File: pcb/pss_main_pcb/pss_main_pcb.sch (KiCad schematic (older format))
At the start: 44 parts

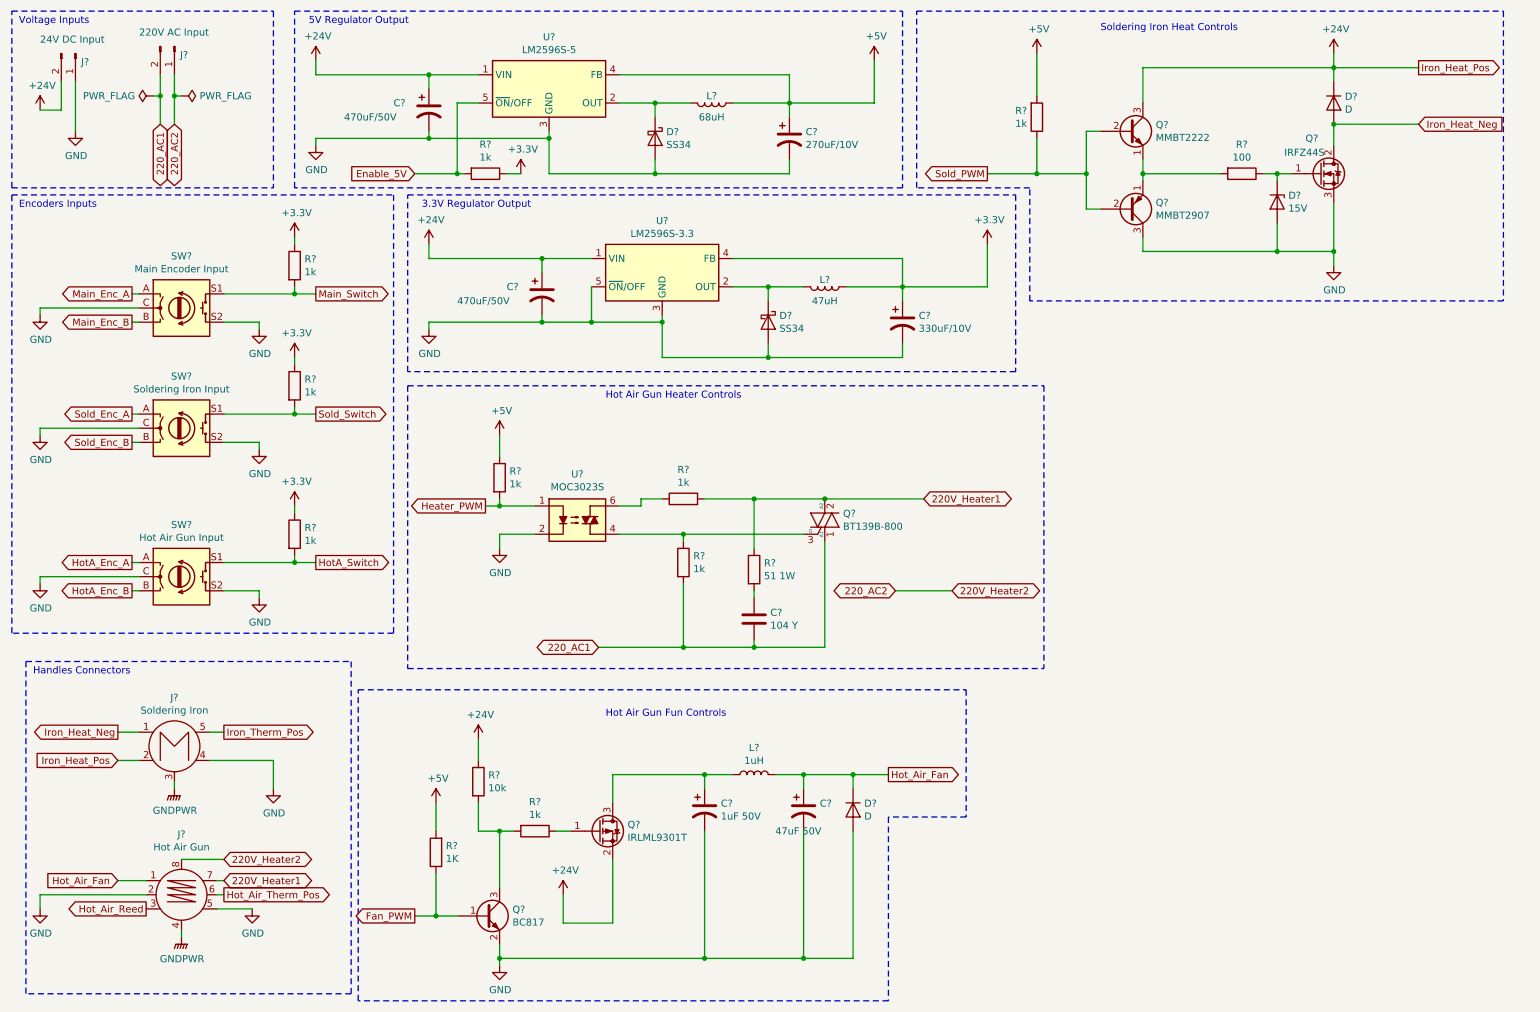
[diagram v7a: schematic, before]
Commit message: Add thermocouple feedback schematics
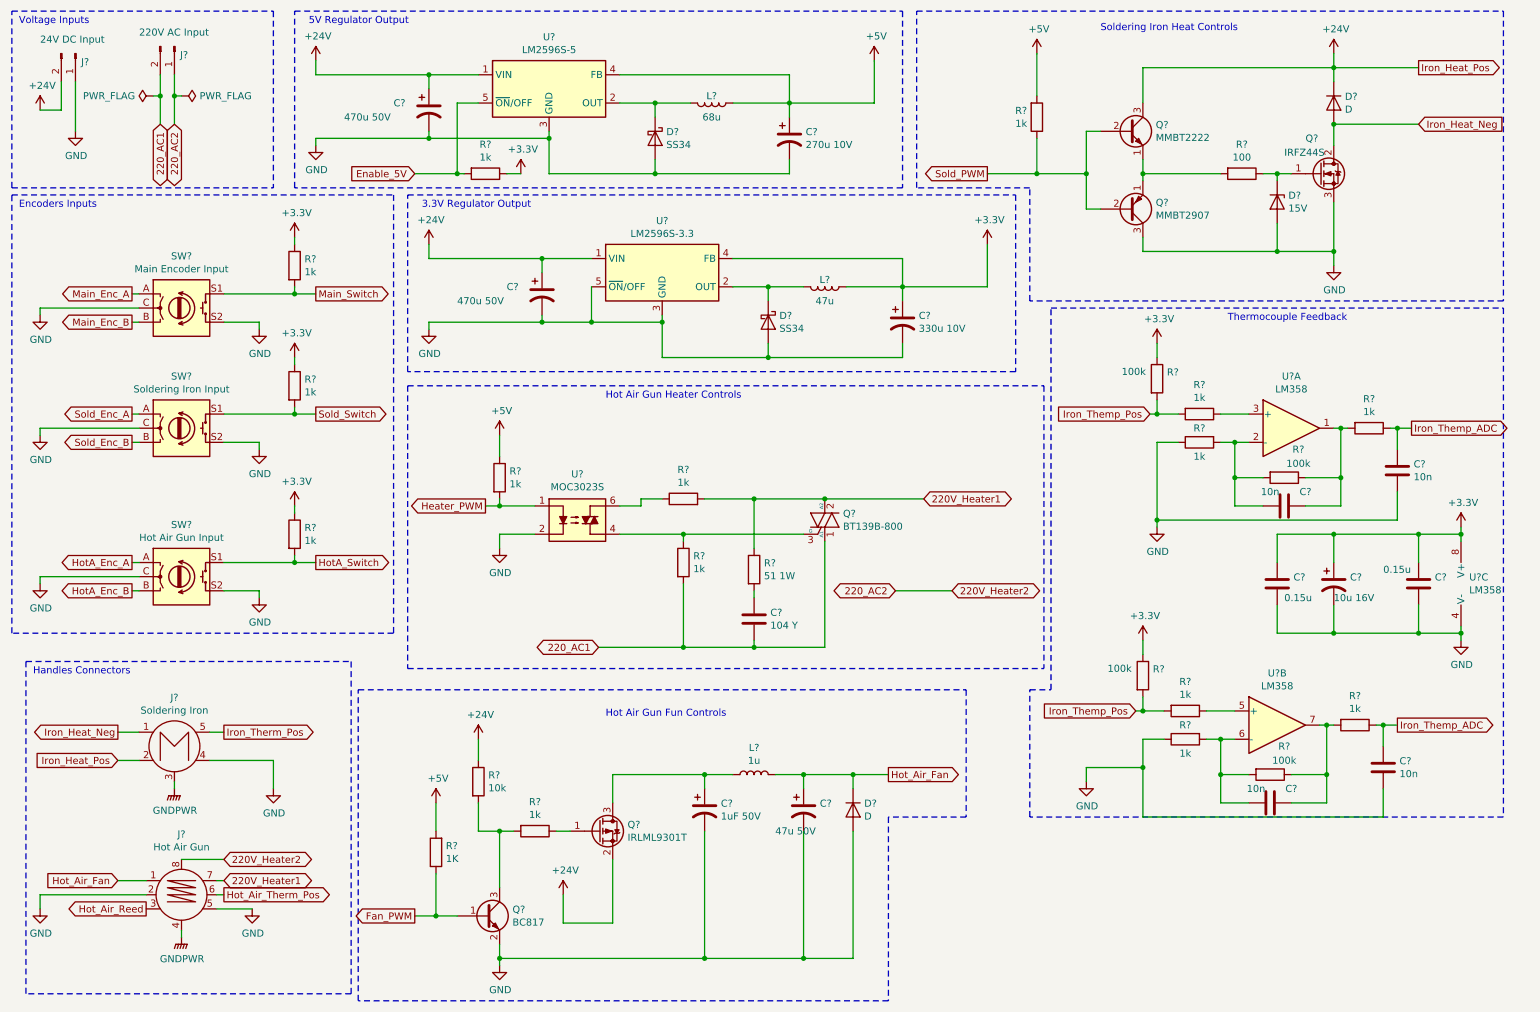
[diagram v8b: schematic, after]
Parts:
- added C? (x2): 0.15u, symbol Device:C
- added C? (x4): 10n, symbol Device:C
- added C?: 10u 16V, symbol Device:CP1
- added R? (x6): 1k, symbol Device:R
- added R? (x4): 100k, symbol Device:R
- added U? (x3): LM358, symbol Amplifier_Operational:LM358
- C? (x2): value 470uF/50V -> 470u 50V
- C?: value 270uF/10V -> 270u 10V
- C?: value 330uF/10V -> 330u 10V
- C?: value 47uF 50V -> 47u 50V
- L?: value 68uH -> 68u
- L?: value 47uH -> 47u
- L?: value 1uH -> 1u
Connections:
- net +3V3: now also C?.1, C?.1, C?.1, R?.1, R?.1, U?.8 (V+)
- net GND: now also C?.2, C?.2, C?.2, C?.2, C?.2, R?.1, R?.1, U?.4 (V-)
- new net: R?.1, U?.5 (+)
- new net: C?.1, R?.2, R?.2, U?.6 (-)
- new net: C?.2, R?.1, R?.2, U?.7
- new net: C?.2, R?.1, R?.2, U?.1
- new net: C?.1, R?.2, R?.2, U?.2 (-)
- new net: R?.1, U?.3 (+)
- new net Iron_Themp_ADC: C?.1, C?.1, R?.1, R?.1
- new net Iron_Themp_Pos: R?.2, R?.2, R?.2, R?.2
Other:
- note added: "Thermocouple Feedback\n"
